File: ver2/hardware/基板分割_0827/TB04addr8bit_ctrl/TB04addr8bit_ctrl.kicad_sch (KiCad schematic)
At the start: 15 parts, among them J1 Conn_02x20_Odd_Even, J1602 Screw_Terminal_01x02, J2 Conn_02x20_Odd_Even, J3 Conn_02x10_Odd_Even, J5 Conn_02x10_Odd_Even, U101 74LS157

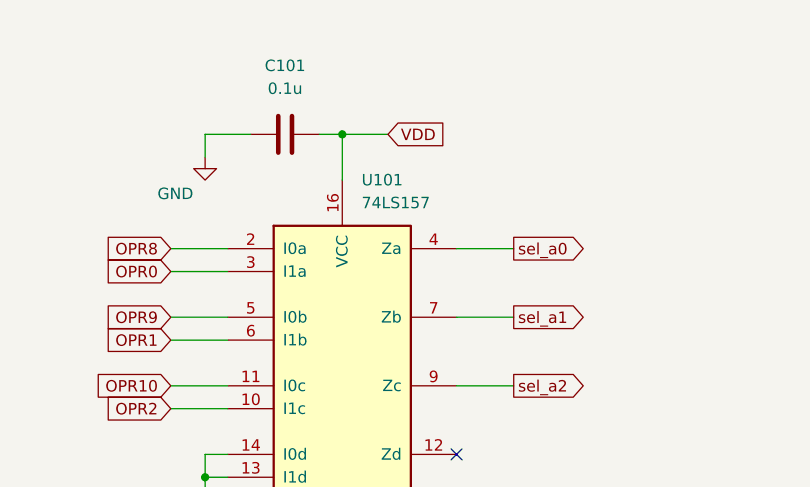
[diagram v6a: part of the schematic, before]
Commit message: ver2: 3分割の74LS表記をHCへ一括変更(31パッケージ・Valueのみ)
- 書き換えたのはValueプロパティのみ(56件=31パッケージ)
- lib_id(74xx:74LS***)とDatasheetは変更せず。HC品のシンボルがKiCADに
  無いため、lib_idを変えるとシンボル未検出になる
- 74LS->74HCの単純置換で9品種すべて実在の型番(00/08/10/32/139/157/
  253/273/377)。ピン配置は同一でネットリストへの影響なし

検証: 残存する74LSのValue 0件、git diffの変更行はValueの56行のみ
申し送り: PCB側のValueは未同期。「回路図からPCBを更新」で解消する

Co-Authored-By: Claude Opus 5 <noreply@anthropic.com>
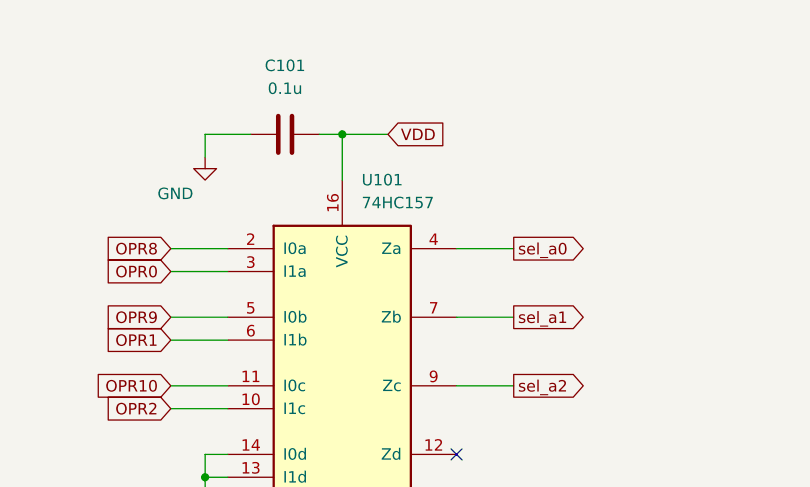
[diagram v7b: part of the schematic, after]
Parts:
- U101: value 74LS157 -> 74HC157
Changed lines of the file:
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@@
 			)
 		)
-		(property "Value" "74LS157"
+		(property "Value" "74HC157"
 			(at 247.2533 53.34 0)
 			(show_name no)

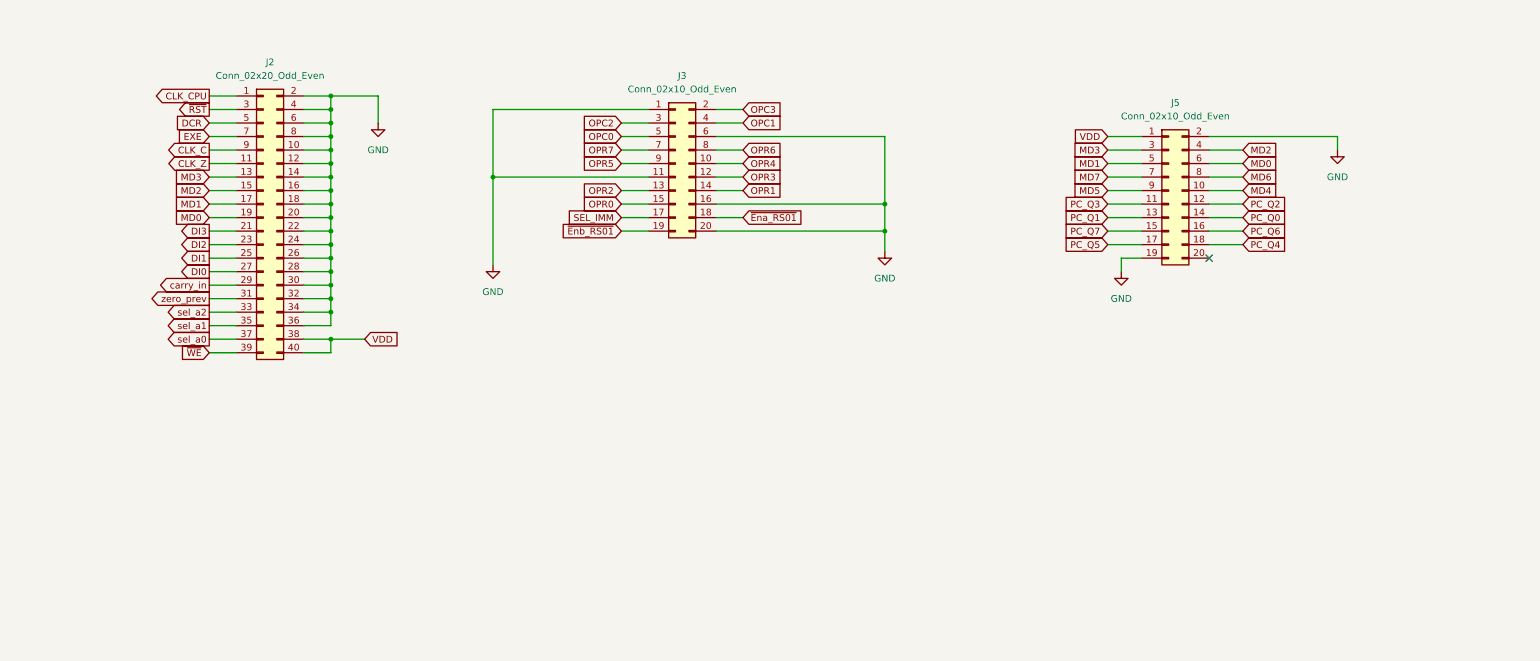
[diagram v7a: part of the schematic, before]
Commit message: ver2: デザインルールを3枚へコピー／制御板の配置を決定(200x180へ拡大)
デザインルール(キャリアで決めた値を_ctrl/_alu/_ifへ):
- 信号0.2mm・電源0.8mm・クリアランス0.2mm・ビア0.6/0.3
- 銅箔-基板端0.5mm、ゾーン最小クリアランス0.5mm

制御板の配置:
- 200x135では部品が55mm分あふれるため200x180へ拡大($16.9->$21.3)
- ブロックの左右はケーブルの向きで決定(J1=IF板/J2,J3=演算板への
  接続本数の差で並べ、ROM_ALUを演算板側の右端へ)
- 並び: ram,addrMUX -> PC_aluMux,sp,addrDecord -> gates -> Decoder -> ROM_ALU
- パスコンは全34ICの1番ピンと電源ピンの間(DIPの上辺)に配置
- 表示8桁を下端に25mmピッチ一列、ケーブルは左右端、電源入口は上端

検証: 外形はみ出し0・courtyard重なり0・パスコン34/34
DRC違反はシルク3件のみ(未配線499は配線前のため)

同梱: 並行して行われた回路図編集(キャリア用2x10を廃し2x5直挿しへ。
制御板はJ5削除、IF板はJ4->J10-J13)

Co-Authored-By: Claude Opus 5 <noreply@anthropic.com>
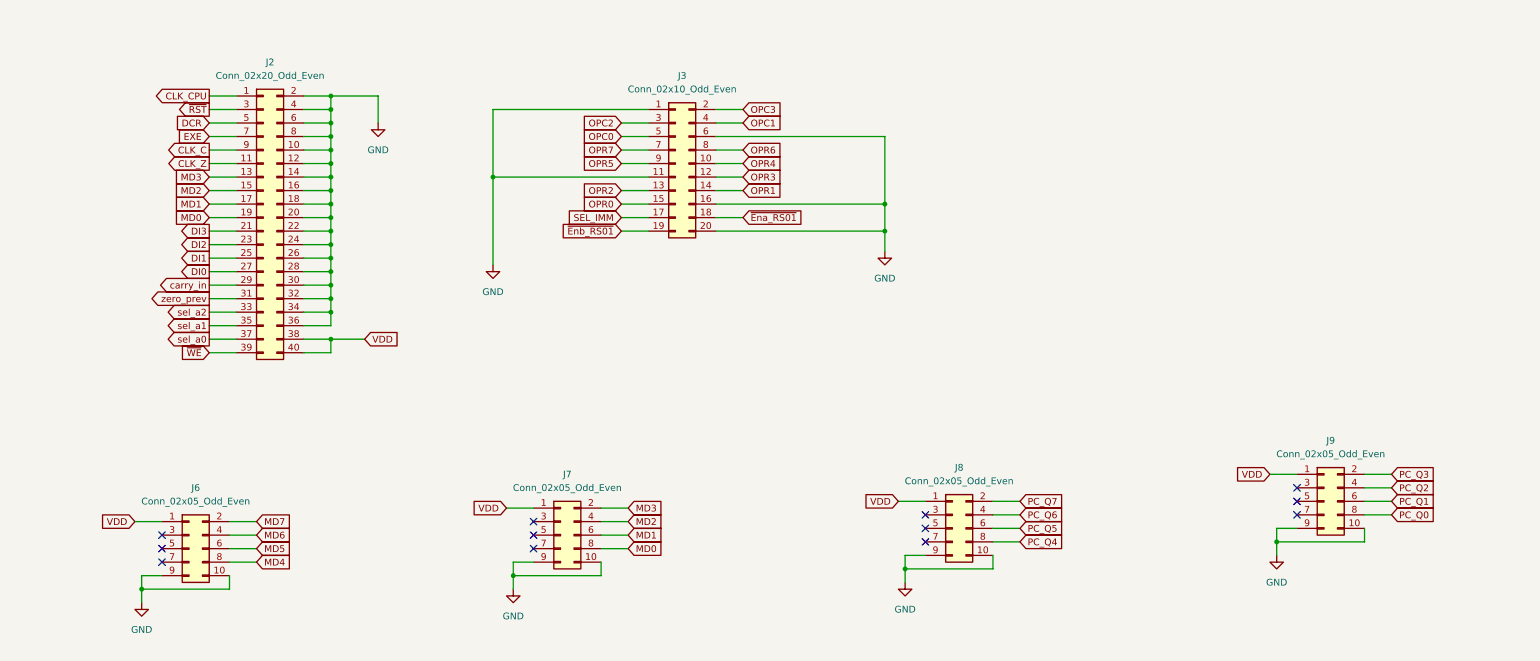
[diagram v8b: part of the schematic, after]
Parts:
- removed J5: Conn_02x10_Odd_Even, Connector_PinSocket_2.54mm:PinSocket_2x10_P2.54mm_Vertical, symbol Connector_Generic:Conn_02x10_Odd_Even
- added J6, J7, J8, J9: Conn_02x05_Odd_Even, Connector_PinSocket_2.54mm:PinSocket_2x05_P2.54mm_Vertical, symbol Connector_Generic:Conn_02x05_Odd_Even
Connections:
- net GND: now also J6.10 (Pin_10), J6.9 (Pin_9), J7.10 (Pin_10), J7.9 (Pin_9), J8.10 (Pin_10), J8.9 (Pin_9), J9.10 (Pin_10), J9.9 (Pin_9)
- net MD0: now also J7.8 (Pin_8)
- net MD1: now also J7.6 (Pin_6)
- net MD2: now also J7.4 (Pin_4)
- net MD3: now also J7.2 (Pin_2)
- net MD4: now also J6.8 (Pin_8)
- net MD5: now also J6.6 (Pin_6)
- net MD6: now also J6.4 (Pin_4)
- net MD7: now also J6.2 (Pin_2)
- net PC_Q0: now also J9.8 (Pin_8)
- net PC_Q1: now also J9.6 (Pin_6)
- net PC_Q2: now also J9.4 (Pin_4)
- net PC_Q3: now also J9.2 (Pin_2)
- net PC_Q4: now also J8.8 (Pin_8)
- net PC_Q5: now also J8.6 (Pin_6)
- net PC_Q6: now also J8.4 (Pin_4)
- net PC_Q7: now also J8.2 (Pin_2)
- net VDD: now also J6.1 (Pin_1), J7.1 (Pin_1), J8.1 (Pin_1), J9.1 (Pin_1)
- no-connect marks 4 -> 15
